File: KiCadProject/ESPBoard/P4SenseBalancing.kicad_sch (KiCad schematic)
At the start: 0 parts

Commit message: ESP board layout mostly done. Small updates to battery management board
Signed-off-by: Eldalote.Electronics <Eldalote.Electronics@gmail.com>
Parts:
- added C401, C402, C403, C404: 1u, Capacitor_SMD:C_0603_1608Metric, symbol Device:C
- added D401, D402, D403, D404: 3v3, Diode_SMD:D_0402_1005Metric, symbol Device:D_TVS
- added Q401, Q403, Q405, Q407: NFET_Gatenames, symbol Eldalote_symbols:NFET_Gatenames
- added Q402, Q404, Q406, Q408: PMOS_Gatenames, symbol Eldalote_symbols:PMOS_Gatenames
- added R401, R402, R404, R405, R407, R408, R410, R411, R413, R418, R419, R420: 10k, Resistor_SMD:R_0402_1005Metric, symbol Device:R
- added R403, R406, R409, R412: 100R, Resistor_SMD:R_0805_2012Metric, symbol Device:R
- added R414, R416: 19k1, Resistor_SMD:R_0402_1005Metric, symbol Device:R
- added R415, R417: 40k2, Resistor_SMD:R_0402_1005Metric, symbol Device:R
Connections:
- new net: Q404.D, R406.1
- new net: Q408.D, R412.1
- new net: Q406.D, R409.1
- new net: Q402.D, R403.1
- new net Cell1: Q408.S, R409.2, R411.1, R413.1
- new net Cell1ADC: C401.1, D401.2 (A2), R413.2, R414.1
- new net Cell1Balance: Q407.G, R410.1
- new net Cell2: Q406.S, R406.2, R408.1, R415.1
- new net Cell2ADC: C402.1, D402.2 (A2), R415.2, R416.1
- new net Cell2Balance: Q405.G, R407.1
- new net Cell3: Q404.S, R403.2, R405.1, R417.1
- new net Cell3ADC: C403.1, D403.2 (A2), R417.2, R418.1
- new net Cell3Balance: Q403.G, R404.1
- new net Cell4: Q402.S, R402.1, R419.1
- new net Cell4ADC: C404.1, D404.2 (A2), R419.2, R420.1
- new net Cell4Balance: Q401.G, R401.1
- new net GND: C401.2, C402.2, C403.2, C404.2, D401.1 (A1), D402.1 (A1), D403.1 (A1), D404.1 (A1), Q401.S, Q403.S, Q405.S, Q407.S, R401.2, R404.2, R407.2, R410.2, R412.2, R414.2, R416.2, R418.2, R420.2
- new net nCell1Balance: Q407.D, Q408.G, R411.2
- new net nCell2Balance: Q405.D, Q406.G, R408.2
- new net nCell3Balance: Q403.D, Q404.G, R405.2
- new net nCell4Balance: Q401.D, Q402.G, R402.2
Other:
- note added: "100k/(100k+19.1k)*20v = 3.21v"
- note added: "10k/(10k+19.1k)*5v = 3.28v"
- note added: "40.2k/(40.2k+10k)*15v = 2.99v"
- note added: "40.2k/(40.2k+19.1k)*10v = 3.22v"
- note added: "ADC limit is 3v3. Each cell is nominally max 4.2v, but 5v is kept as a safety margin each resistor devider aims to get the max voltage (5, 10, 15, 20) as close to 3v3 as reasonable without going over. Exact match in ratios not needed, can be calibrated after assembly"
- note added: "ESD diodes behind the resistor divider is not ideal, but it saves significantly on BOM."
- note added: "From Page 2"
- note added: "To/From Page 3"

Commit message: Tweaking
Signed-off-by: Eldalote.Electronics <Eldalote.Electronics@gmail.com>
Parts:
- Q401, Q402, Q403, Q404, Q405, Q406, Q407, Q408: footprint (none) -> Package_TO_SOT_SMD:SOT-23
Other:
- note added: "ADC limit is 3v3. Each cell is nominally max 4.2v, but 5v is kept as a safety margin each resistor devider aims to get the max voltage (5, 10, 15, 20) as close to 3v3 as reasonable without going over. Exact match in ratios not needed, can be calibrated after assembly With the selected values, only 2 new resistor values are needed."
- note removed: "ADC limit is 3v3. Each cell is nominally max 4.2v, but 5v is kept as a safety margin each resistor devider aims to get the max voltage (5, 10, 15, 20) as close to 3v3 as reasonable without going over. Exact match in ratios not needed, can be calibrated after assembly"
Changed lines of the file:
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@@
     (effects (font (size 1.27 1.27)) (justify left bottom))
   )
-  (text "ADC limit is 3v3.\nEach cell is nominally max 4.2v, but 5v is kept as a safety margin\n\neach resistor devider aims to get the max voltage (5, 10, 15, 20) as close to 3v3 as\nreasonable without going over.\n\nExact match in ratios not needed, can be calibrated after assembly"
-    (at 180.34 43.18 0)
+  (text "ADC limit is 3v3.\nEach cell is nominally max 4.2v, but 5v is kept as a safety margin\n\neach resistor devider aims to get the max voltage (5, 10, 15, 20) as close to 3v3 as\nreasonable without going over.\n\nExact match in ratios not needed, can be calibrated after assembly\n\nWith the selected values, only 2 new resistor values are needed."
+    (at 190.5 52.07 0)
     (effects (font (size 1.27 1.27)) (justify left bottom))
   )
@@
       (effects (font (size 1.27 1.27)) hide)
     )
-    (property "Footprint" "" (id 2) (at 101.6 90.17 0)
+    (property "Footprint" "Package_TO_SOT_SMD:SOT-23" (id 2) (at 101.6 90.17 0)
       (effects (font (size 1.27 1.27)) hide)
     )
@@
       (effects (font (size 1.27 1.27)) hide)
     )
-    (property "Footprint" "" (id 2) (at 118.11 147.32 0)
+    (property "Footprint" "Package_TO_SOT_SMD:SOT-23" (id 2) (at 118.11 147.32 0)
       (effects (font (size 1.27 1.27)) hide)
     )
@@
       (effects (font (size 1.27 1.27)) hide)
     )
-    (property "Footprint" "" (id 2) (at 101.6 58.42 0)
+    (property "Footprint" "Package_TO_SOT_SMD:SOT-23" (id 2) (at 101.6 58.42 0)
       (effects (font (size 1.27 1.27)) hide)
     )
@@
       (effects (font (size 1.27 1.27)) hide)
     )
-    (property "Footprint" "" (id 2) (at 118.11 115.57 0)
+    (property "Footprint" "Package_TO_SOT_SMD:SOT-23" (id 2) (at 118.11 115.57 0)
       (effects (font (size 1.27 1.27)) hide)
     )
@@
       (effects (font (size 1.27 1.27)) hide)
     )
-    (property "Footprint" "" (id 2) (at 118.11 52.07 0)
+    (property "Footprint" "Package_TO_SOT_SMD:SOT-23" (id 2) (at 118.11 52.07 0)
       (effects (font (size 1.27 1.27)) hide)
     )
@@
       (effects (font (size 1.27 1.27)) hide)
     )
-    (property "Footprint" "" (id 2) (at 101.6 121.92 0)
+    (property "Footprint" "Package_TO_SOT_SMD:SOT-23" (id 2) (at 101.6 121.92 0)
       (effects (font (size 1.27 1.27)) hide)
     )
@@
       (effects (font (size 1.27 1.27)) hide)
     )
-    (property "Footprint" "" (id 2) (at 118.11 83.82 0)
+    (property "Footprint" "Package_TO_SOT_SMD:SOT-23" (id 2) (at 118.11 83.82 0)
       (effects (font (size 1.27 1.27)) hide)
     )
@@
       (effects (font (size 1.27 1.27)) hide)
     )
-    (property "Footprint" "" (id 2) (at 101.6 153.67 0)
-      (effects (font (size 1.27 1.27)) hide)
-    )
+    (property "Footprint" "Package_TO_SOT_SMD:SOT-23" (id 2) (at 101.6 153.67 0)
+      (effects (font (size 1.27 1.27)) hide)
+    )

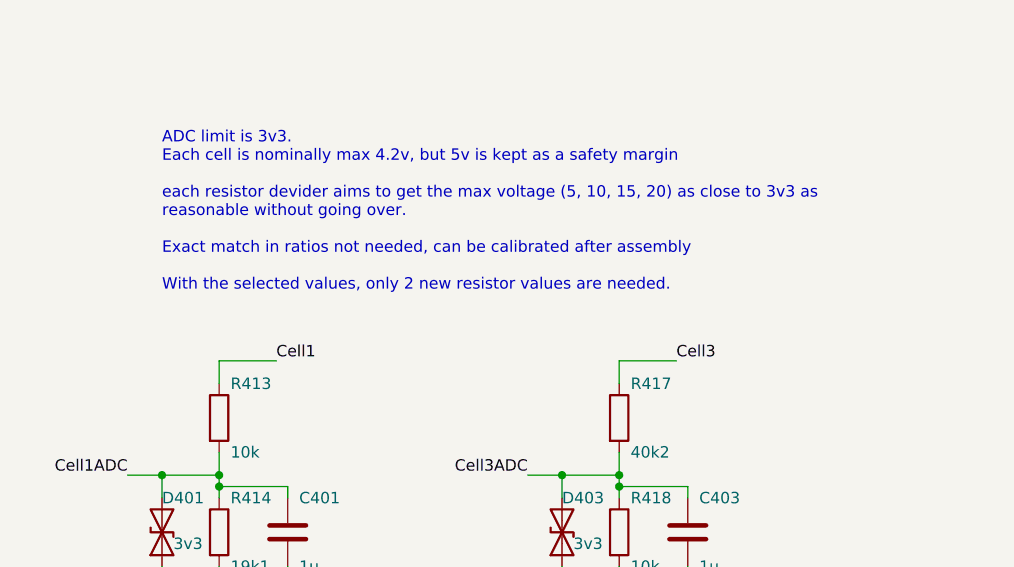
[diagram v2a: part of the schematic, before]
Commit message: Components selected, MfID added to schematics, and components ordered
Signed-off-by: Eldalote.Electronics <Eldalote.Electronics@gmail.com>
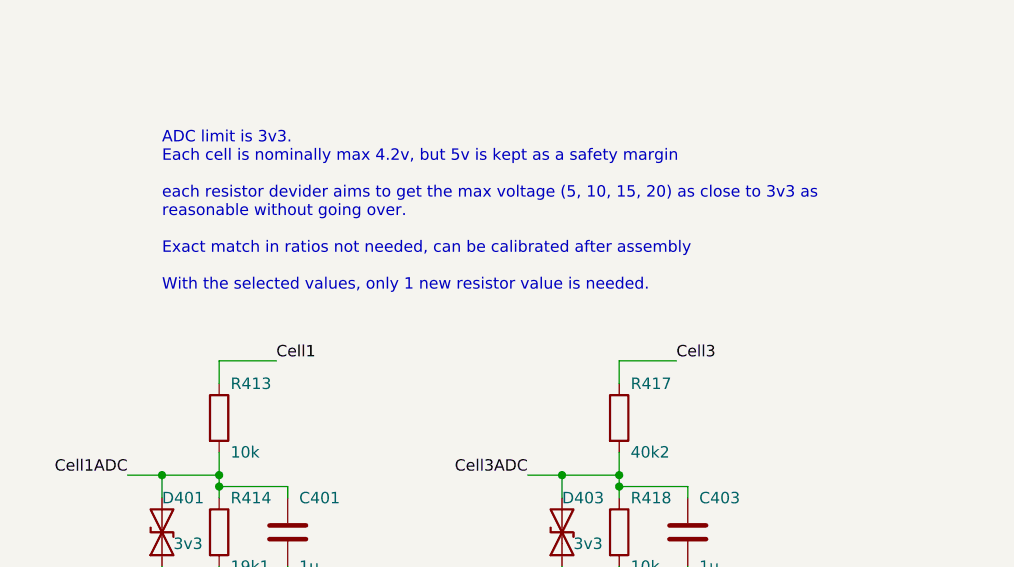
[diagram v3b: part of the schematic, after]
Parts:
- C401, C402, C403, C404: MfID (none) -> CL10A105KA8NNNC
- D401, D402, D403, D404: footprint Diode_SMD:D_0402_1005Metric -> Diode_SMD:D_SOD-523; MfID (none) -> ESD3V3D5
- Q401, Q403, Q405, Q407: footprint Package_TO_SOT_SMD:SOT-23 -> (none); MfID (none) -> RE1C002UNTCL
- Q402, Q404, Q406, Q408: footprint Package_TO_SOT_SMD:SOT-23 -> (none); Extra Requirement (none) -> min 100mA Ta; MfID (none) -> SSM3J35AMFV,L3F
- R401, R402, R404, R405, R407, R408, R410, R411, R413, R418, R419, R420: MfID (none) -> CR0402-FX-1002GLF
- R403, R406, R409, R412: Extra Requirement (none) -> min 1/4 watt; MfID (none) -> RK73H2ATTD1000F
- R414, R416: MfID (none) -> RC0402FR-0719K1L
- R415, R417: MfID (none) -> CR0402-FX-4022GLF
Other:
- note added: "ADC limit is 3v3. Each cell is nominally max 4.2v, but 5v is kept as a safety margin each resistor devider aims to get the max voltage (5, 10, 15, 20) as close to 3v3 as reasonable without going over. Exact match in ratios not needed, can be calibrated after assembly With the selected values, only 1 new resistor value is needed."
- note removed: "ADC limit is 3v3. Each cell is nominally max 4.2v, but 5v is kept as a safety margin each resistor devider aims to get the max voltage (5, 10, 15, 20) as close to 3v3 as reasonable without going over. Exact match in ratios not needed, can be calibrated after assembly With the selected values, only 2 new resistor values are needed."

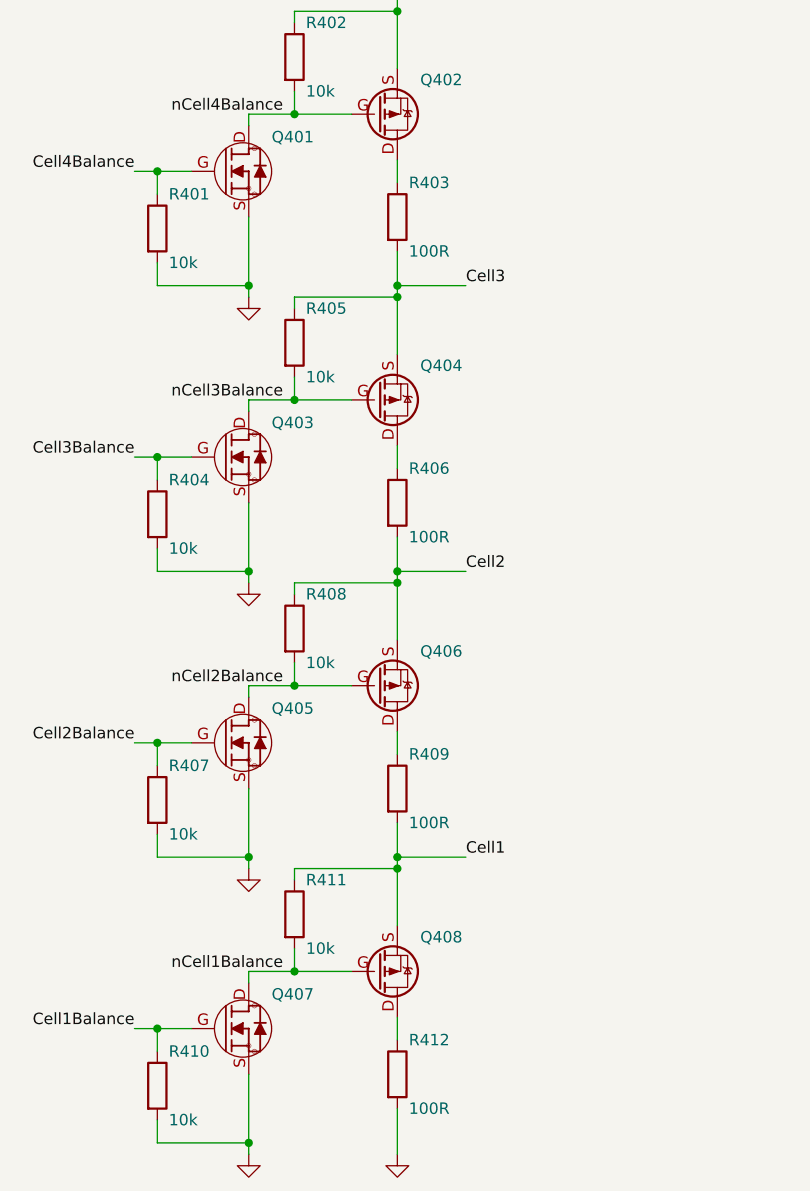
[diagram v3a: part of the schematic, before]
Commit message: Finished v0.1 of BatMan PCB, started layout of ESP PCB
Signed-off-by: Eldalote.Electronics <Eldalote.Electronics@gmail.com>
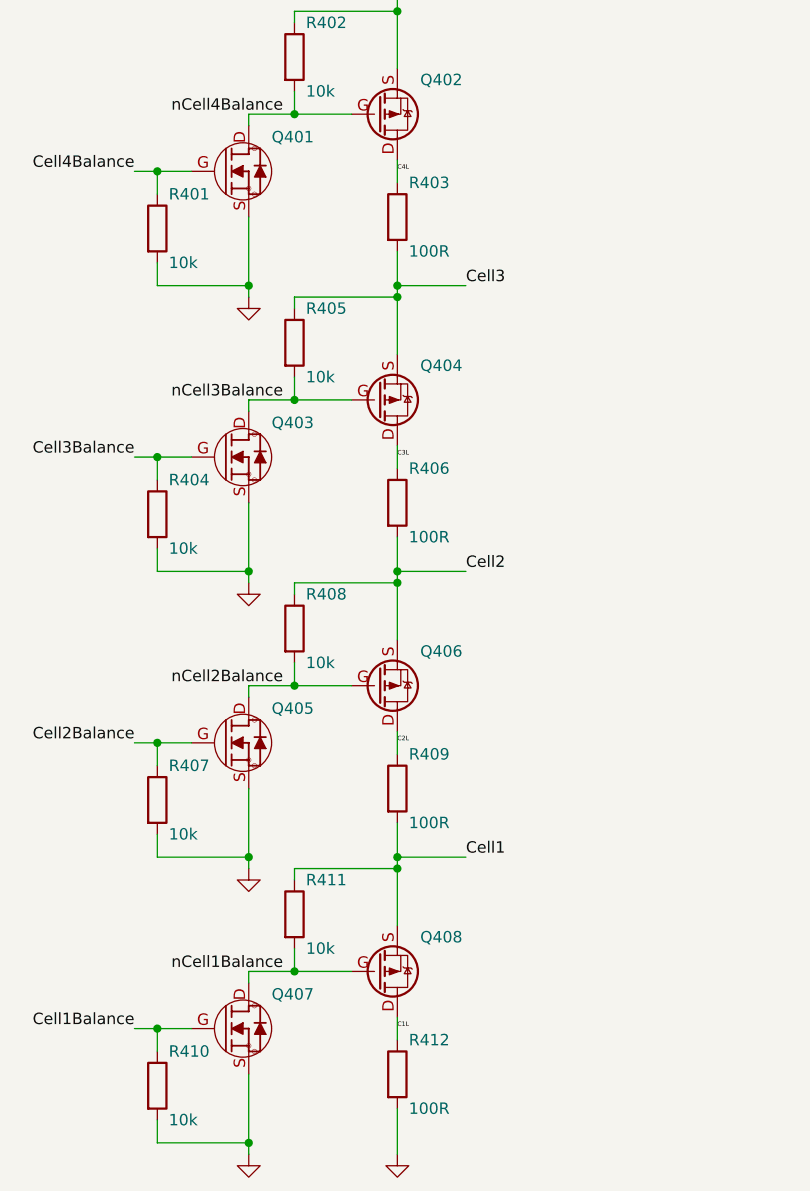
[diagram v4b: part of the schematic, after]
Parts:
- Q401, Q403, Q405, Q407: footprint (none) -> Eldalote-footprints:SC-89(GSD)
- Q402, Q404, Q406, Q408: footprint (none) -> Eldalote-footprints:SOT-723(GSD)
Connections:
- net C3L: now reaches Q404.D, R406.1
- net C1L: now reaches Q408.D, R412.1
- net C2L: now reaches Q406.D, R409.1
- net C4L: now reaches Q402.D, R403.1
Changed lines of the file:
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@@
     (effects (font (size 1.27 1.27)) (justify left bottom))
+  )
+  (label "C2L" (at 118.11 121.92 0)
+    (effects (font (size 0.5 0.5)) (justify left bottom))
   )
   (label "Cell1ADC" (at 186.69 72.39 180)
     (effects (font (size 1.27 1.27)) (justify right bottom))
   )
+  (label "C4L" (at 118.11 58.42 0)
+    (effects (font (size 0.5 0.5)) (justify left bottom))
+  )
   (label "Cell3ADC" (at 35.56 54.61 0)
     (effects (font (size 1.27 1.27)) (justify left bottom))
@@
     (effects (font (size 1.27 1.27)) (justify left bottom))
   )
+  (label "C1L" (at 118.11 153.67 0)
+    (effects (font (size 0.5 0.5)) (justify left bottom))
+  )
   (label "Cell2ADC" (at 185.42 115.57 180)
     (effects (font (size 1.27 1.27)) (justify right bottom))
@@
     (effects (font (size 1.27 1.27)) (justify left bottom))
   )
+  (label "C3L" (at 118.11 90.17 0)
+    (effects (font (size 0.5 0.5)) (justify left bottom))
+  )
   (label "Cell2Balance" (at 88.9 121.92 180)
     (effects (font (size 1.27 1.27)) (justify right bottom))
@@
       (effects (font (size 1.27 1.27)) hide)
     )
-    (property "Footprint" "" (id 2) (at 101.6 90.17 0)
+    (property "Footprint" "Eldalote-footprints:SC-89(GSD)" (id 2) (at 101.6 90.17 0)
       (effects (font (size 1.27 1.27)) hide)
     )
@@
       (effects (font (size 1.27 1.27)) hide)
     )
-    (property "Footprint" "" (id 2) (at 118.11 147.32 0)
+    (property "Footprint" "Eldalote-footprints:SOT-723(GSD)" (id 2) (at 118.11 147.32 0)
       (effects (font (size 1.27 1.27)) hide)
     )
@@
       (effects (font (size 1.27 1.27)) hide)
     )
-    (property "Footprint" "" (id 2) (at 101.6 58.42 0)
+    (property "Footprint" "Eldalote-footprints:SC-89(GSD)" (id 2) (at 101.6 58.42 0)
       (effects (font (size 1.27 1.27)) hide)
     )
@@
       (effects (font (size 1.27 1.27)) hide)
     )
-    (property "Footprint" "" (id 2) (at 118.11 115.57 0)
+    (property "Footprint" "Eldalote-footprints:SOT-723(GSD)" (id 2) (at 118.11 115.57 0)
       (effects (font (size 1.27 1.27)) hide)
     )
@@
       (effects (font (size 1.27 1.27)) hide)
     )
-    (property "Footprint" "" (id 2) (at 118.11 52.07 0)
+    (property "Footprint" "Eldalote-footprints:SOT-723(GSD)" (id 2) (at 118.11 52.07 0)
       (effects (font (size 1.27 1.27)) hide)
     )
@@
       (effects (font (size 1.27 1.27)) hide)
     )
-    (property "Footprint" "" (id 2) (at 101.6 121.92 0)
+    (property "Footprint" "Eldalote-footprints:SC-89(GSD)" (id 2) (at 101.6 121.92 0)
       (effects (font (size 1.27 1.27)) hide)
     )
@@
       (effects (font (size 1.27 1.27)) hide)
     )
-    (property "Footprint" "" (id 2) (at 118.11 83.82 0)
+    (property "Footprint" "Eldalote-footprints:SOT-723(GSD)" (id 2) (at 118.11 83.82 0)
       (effects (font (size 1.27 1.27)) hide)
     )
@@
       (effects (font (size 1.27 1.27)) hide)
     )
-    (property "Footprint" "" (id 2) (at 101.6 153.67 0)
-      (effects (font (size 1.27 1.27)) hide)
-    )
+    (property "Footprint" "Eldalote-footprints:SC-89(GSD)" (id 2) (at 101.6 153.67 0)
+      (effects (font (size 1.27 1.27)) hide)
+    )

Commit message: Made ready to order PCBs. Some problems with ordering due to misunderstanding. Thinking about solutions
Signed-off-by: Eldalote.Electronics <Eldalote.Electronics@gmail.com>
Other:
- company: (none) -> Eldalote Electronics
- title: (none) -> ESP & Feedback Board
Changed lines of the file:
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@@
 (kicad_sch (version 20211123) (generator eeschema)
   (paper "A4")
+  (title_block
+    (title "ESP & Feedback Board")
+    (date "2023-02-02")
+    (rev "0.2")
+    (company "Eldalote Electronics")
+    (comment 2 "Part of the Dive Lamp Design")
+  )
   (junction (at 198.12 85.09) (diameter 0) (color 0 0 0 0)
   )
